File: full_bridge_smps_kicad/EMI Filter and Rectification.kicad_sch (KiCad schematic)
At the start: 52 parts, among them J4 Conn_01x04_Male, J6 Conn_01x04_Male, J7 Conn_01x02_Male, J8 Conn_01x02_Male, Q1 IPW60R041C6, Q1 MMBT2904, Q2 IPW60R041C6, Q2 MMBT2904, Q3 IPW60R041C6, Q4 IPW60R041C6, SW1 SW_SPST, U2 UCC27323D

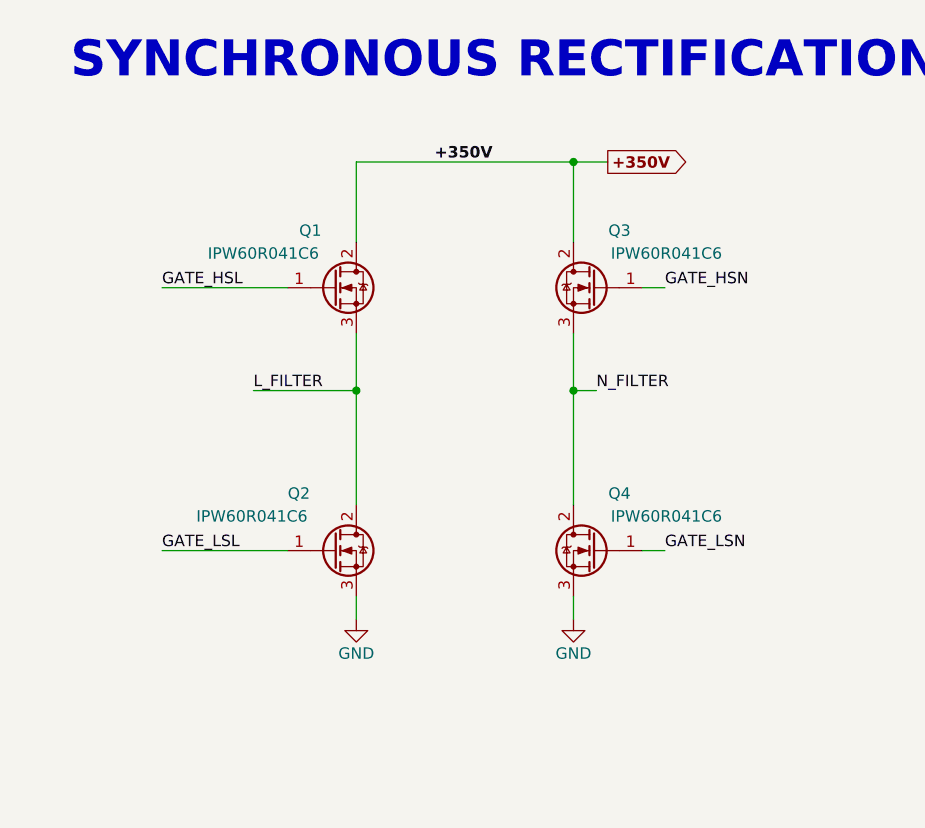
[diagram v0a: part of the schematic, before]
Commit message: Adding schematic page for interleaved CCM PFC
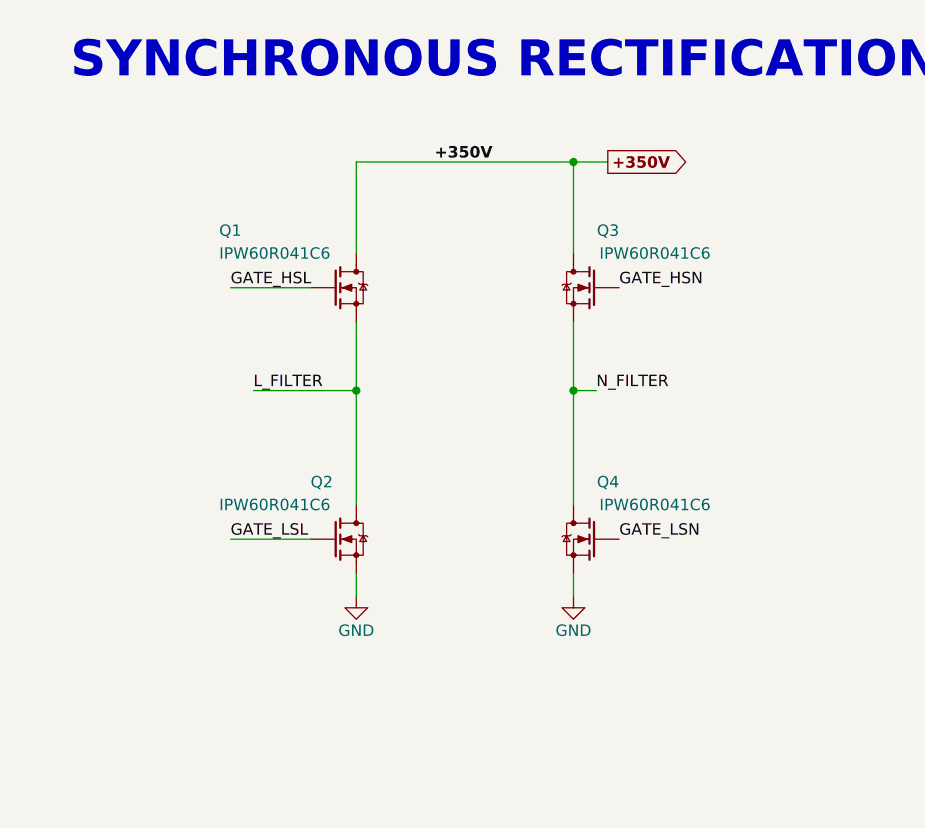
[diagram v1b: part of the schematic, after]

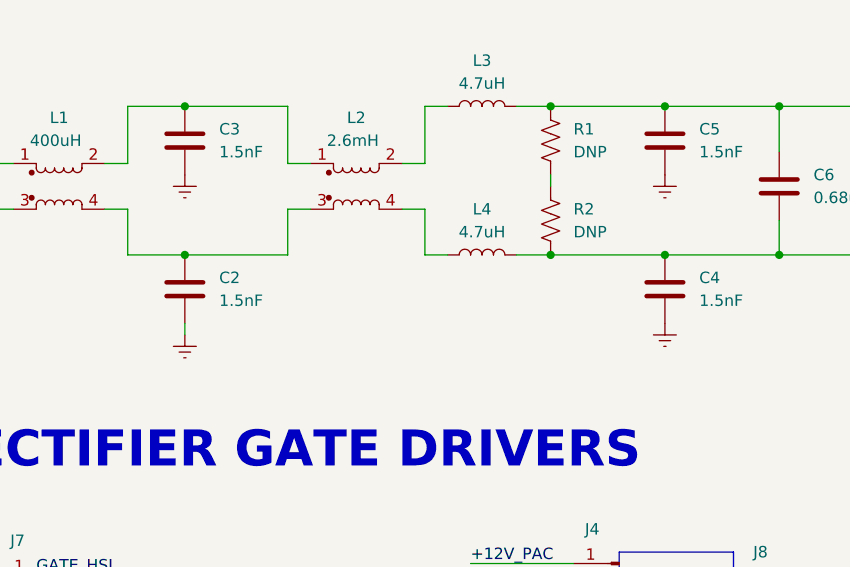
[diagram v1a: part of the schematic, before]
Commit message: Finishing power factor correction sheets, moving to power conversion
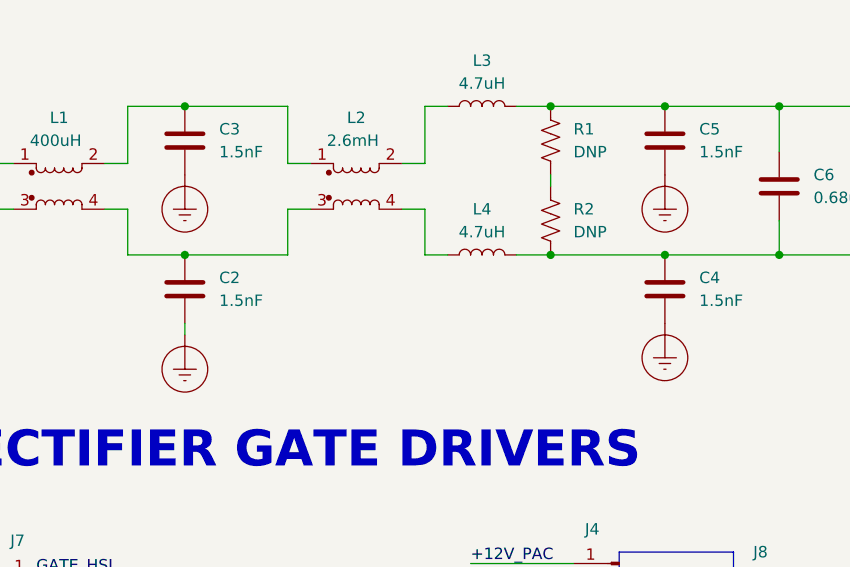
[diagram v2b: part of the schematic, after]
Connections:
- net Earth: no longer C2.2, C3.2, C4.2, C5.2
- new net Earth_Protective: C2.2, C3.2, C4.2, C5.2

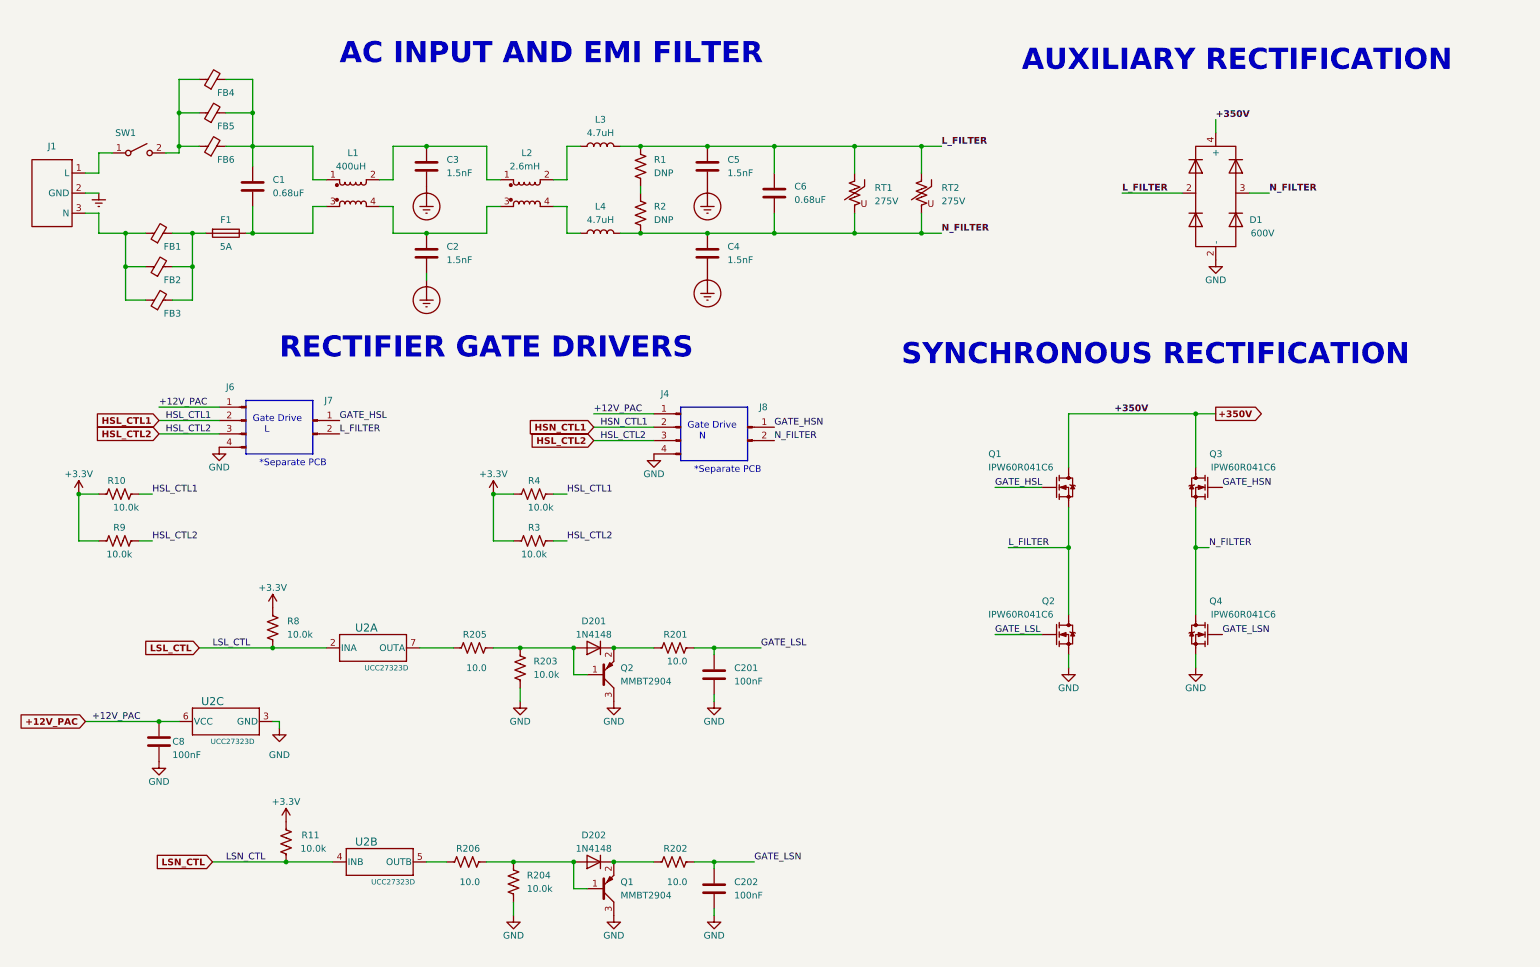
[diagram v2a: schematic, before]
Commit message: Finishing up the output rectification, creating new pages for the corresponding feedback and drive circuits
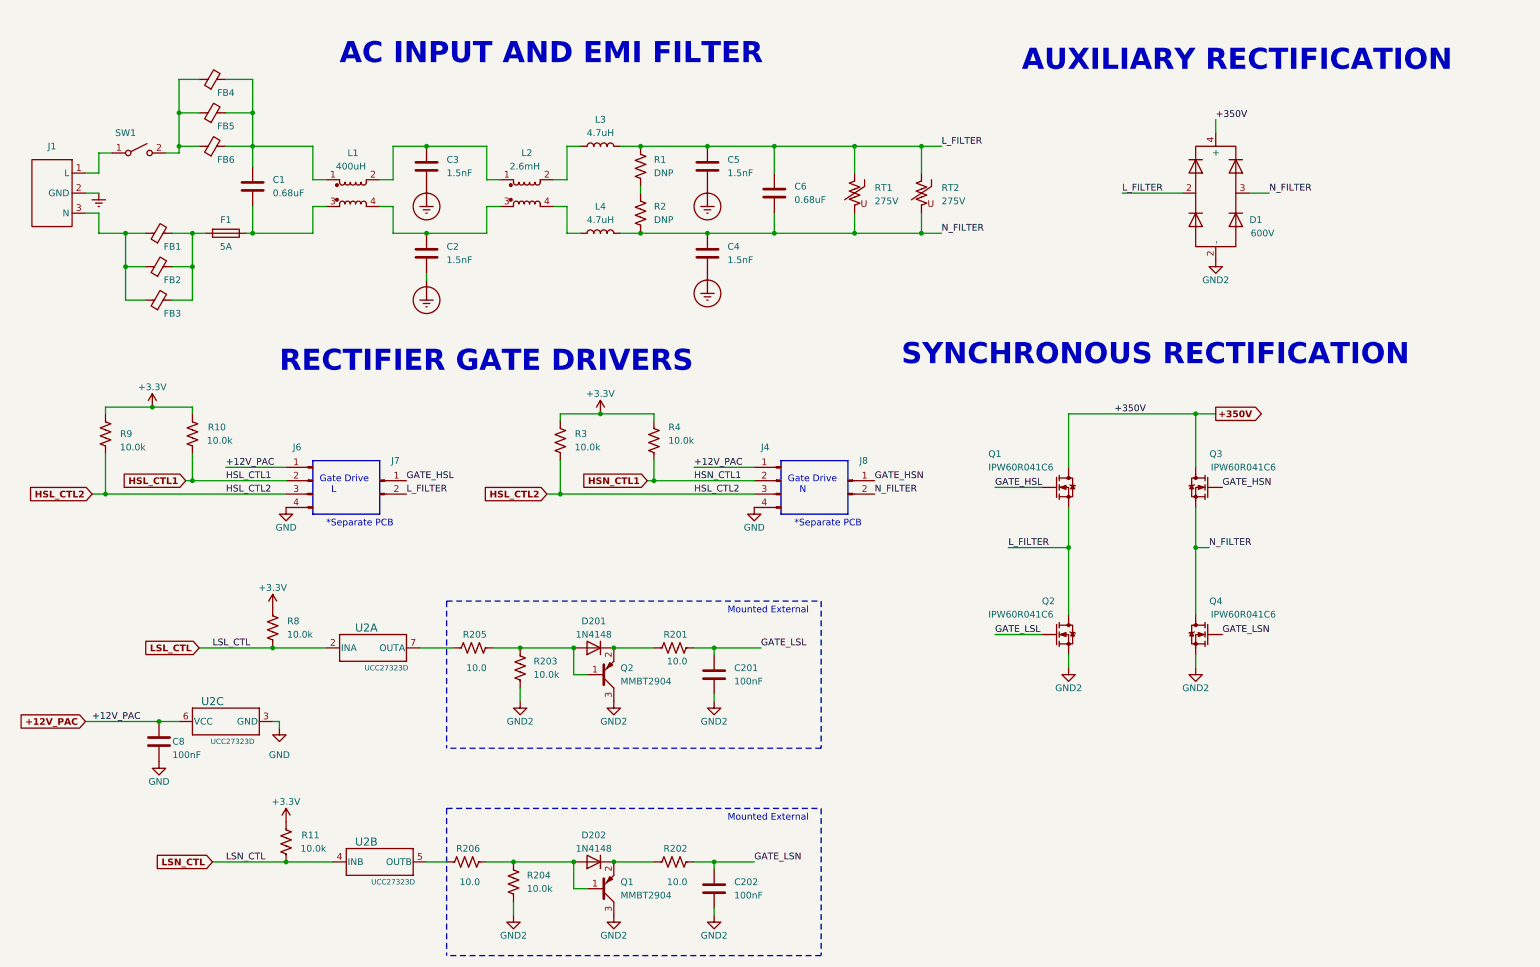
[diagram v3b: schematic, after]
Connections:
- net +3V3: now also R10.2, R3.2, R4.2, R9.2; no longer R10.1, R3.1, R4.1, R9.1
- net GND: no longer C201.2, C202.2, D1.2, Q1.3 (C), Q2.3 (C), Q2.3 (S), Q4.3 (S), R203.2, R204.2
- net HSL_CTL1: now also R10.1; no longer R10.2, R4.2
- net HSL_CTL2: now also R3.1, R9.1; no longer R3.2, R9.2
- net HSN_CTL1: now also R4.1
- new net GND2: C201.2, C202.2, D1.2, Q1.3 (C), Q2.3 (C), Q2.3 (S), Q4.3 (S), R203.2, R204.2
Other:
- note added: "Mounted External"
- moved on the sheet: J4, J6, J7, J8, R10, R3, R4, R9

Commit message: A bit of refactoring, saving work for the day
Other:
- moved on the sheet: C201, C202, C8, D201, D202, J4, J6, J7, J8, Q1, Q2, Q3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
